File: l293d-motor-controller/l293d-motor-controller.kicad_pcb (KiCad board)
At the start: 2 copper layers, 49.6 x 66 mm, 19 parts, among them M1 Motor_DC, M2 Motor_DC, U1 LM7805, U2 L293D, U3 74HC04

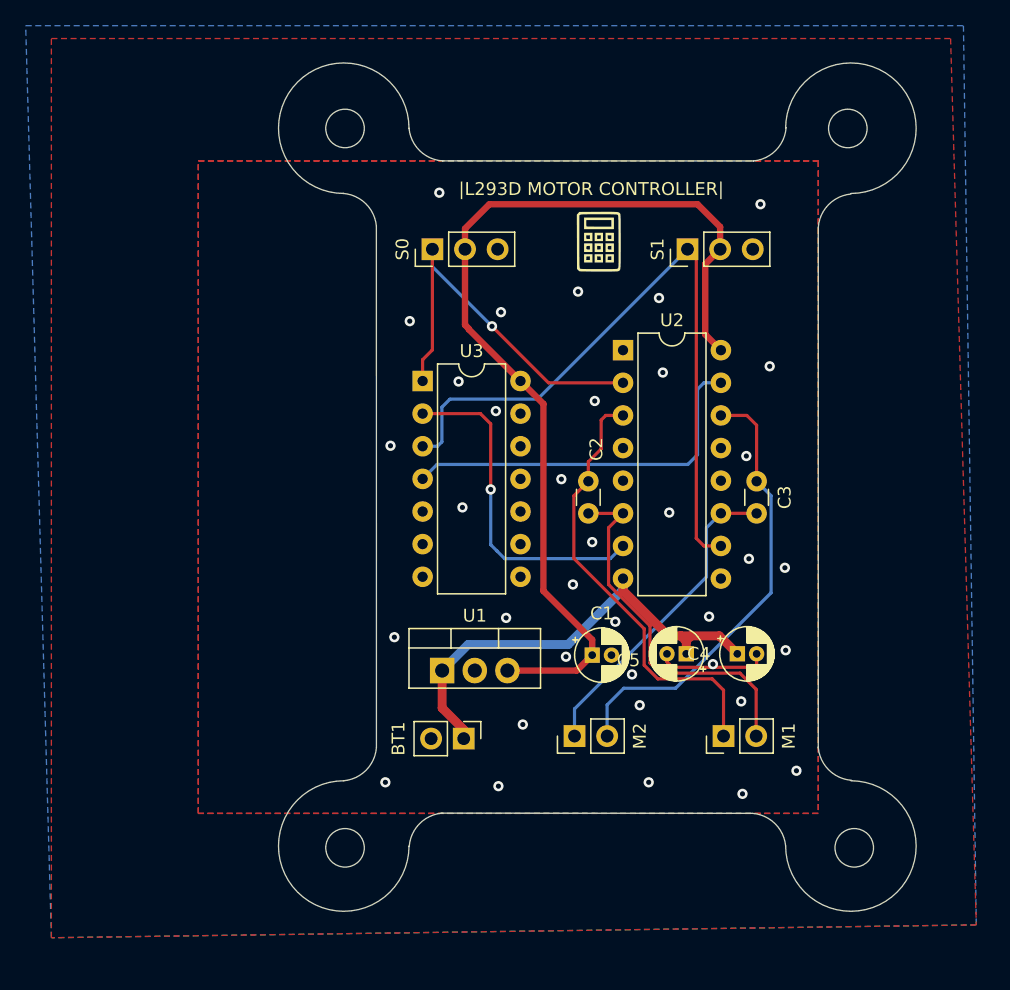
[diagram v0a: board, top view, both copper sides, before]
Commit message: project 3 / l293d motor driver / design improved
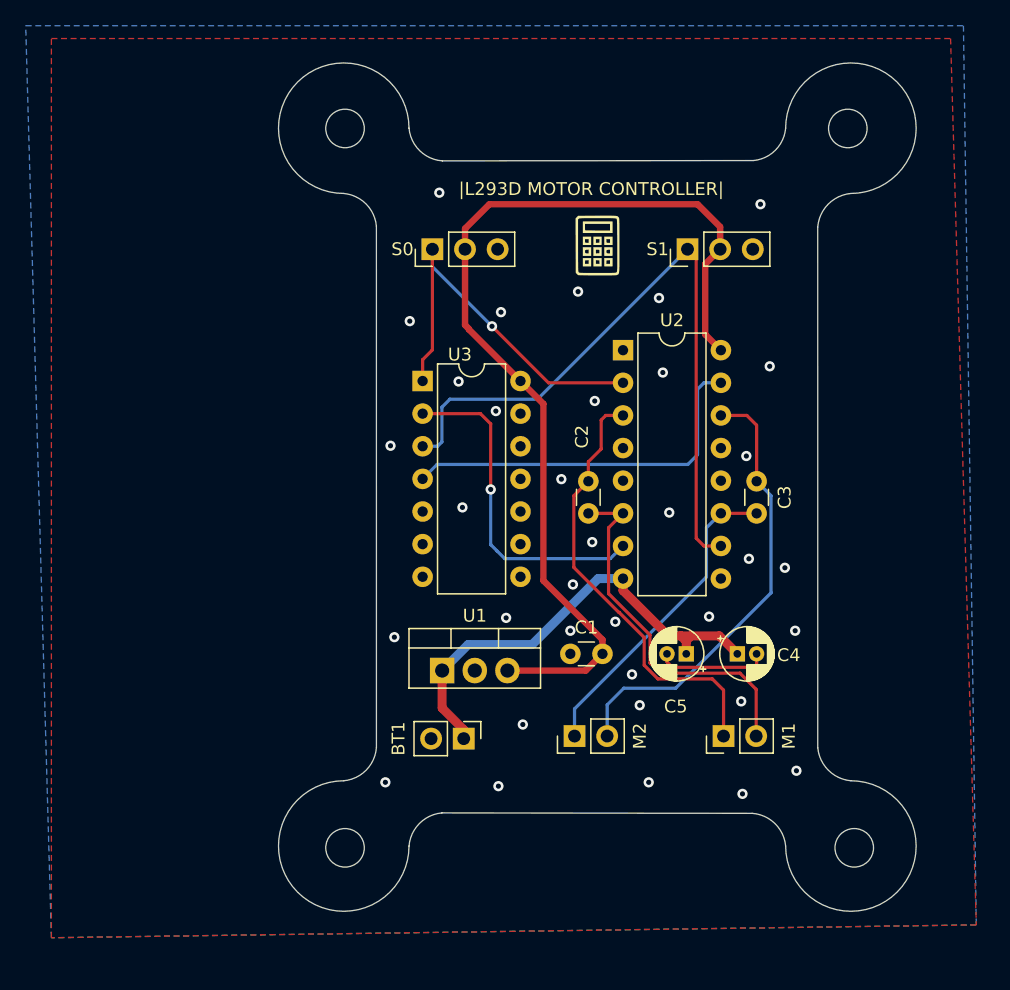
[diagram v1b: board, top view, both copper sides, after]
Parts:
- C1: value C_Polarized -> 100n; footprint Capacitor_THT:CP_Radial_D4.0mm_P1.50mm -> Capacitor_THT:C_Disc_D3.0mm_W1.6mm_P2.50mm
- C2, C3: value C -> 0.01u
- C4: value C_Polarized -> 10u
- C5: value C_Polarized -> 100u
- moved G*** 8.01 mm to (122.3, 122.3), turned to 180 degrees
- moved C1 1.70 mm to (120.4, 134.9)
- moved G*** 0.32 mm to (122.5, 103.1)
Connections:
- C1 pad 1: /5V -> /GND
- C1 pad 2: /GND -> /5V
- C2 pad 2: /VCC -> Net-(M1--)
- M1 pad 2: /VCC -> Net-(M1--)
- U2 pad 6: /VCC -> Net-(M1--)
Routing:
- net /VCC: track 66.5 -> 37.1 mm
- net Net-(M1--): track 0.00 -> 28.9 mm
- net /5V: track 77.1 -> 78.1 mm
- net /GND: track 8.92 -> 8.71 mm, vias 36 -> 35
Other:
- outline, holes or cut-outs redrawn

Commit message: project 3 / l293d motor driver / layout improvement
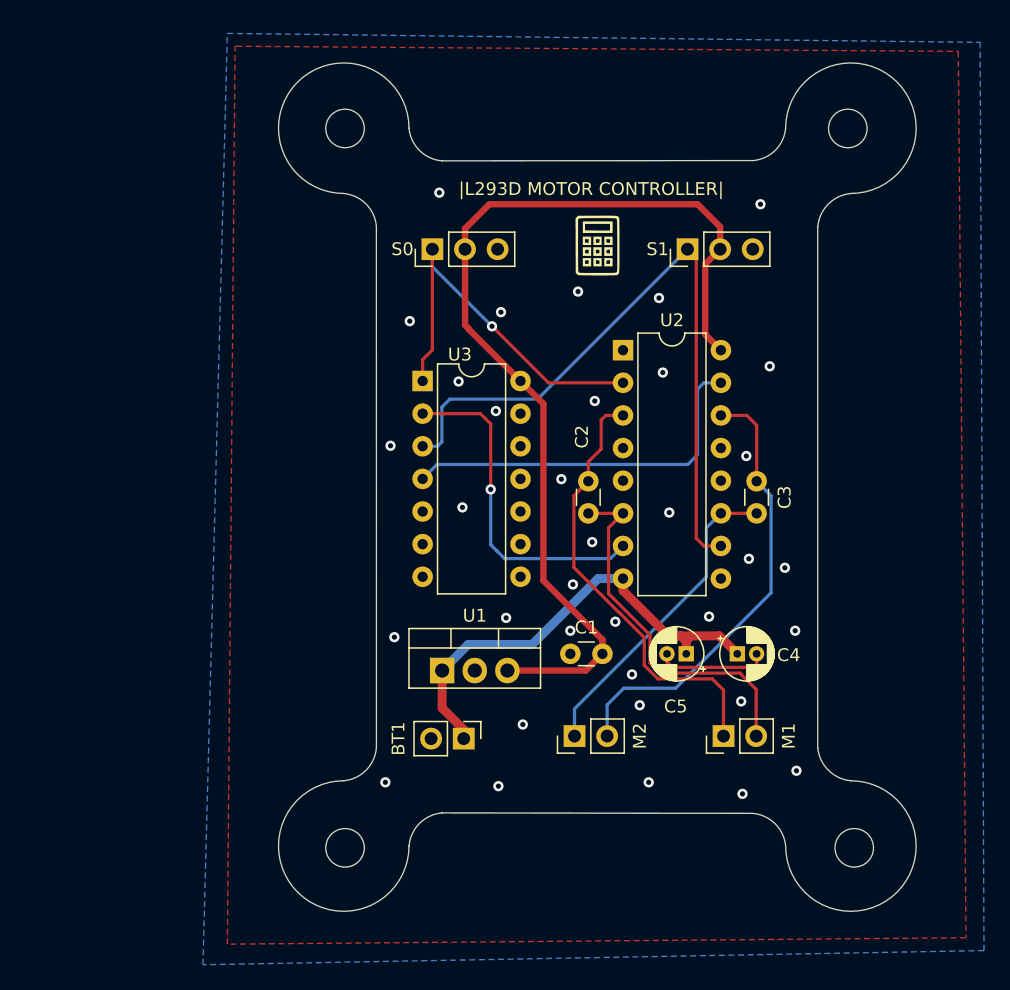
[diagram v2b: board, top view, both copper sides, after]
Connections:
- net /5V renamed +5V
- net /GND renamed GND
- net /VCC renamed +9V
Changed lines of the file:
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@@
   )
   (net 0 "")
-  (net 1 "/VCC")
-  (net 2 "/GND")
+  (net 1 "+9V")
+  (net 2 "GND")
   (net 3 "Net-(M1-+)")
   (net 4 "Net-(M2-+)")
@@
   (net 16 "unconnected-(U3-Q6-Pad12)")
   (net 17 "unconnected-(U3-Q7-Pad13)")
-  (net 18 "/5V")
+  (net 18 "+5V")
   (net 19 "unconnected-(U2-EN3,4-Pad9)")
   (net 20 "unconnected-(U2-EN1,2-Pad1)")
@@
       (stroke (width 0.1) (type solid)) (layer "F.Fab"))
     (pad "1" thru_hole rect (at 0 0) (size 1.905 2) (drill 1.1) (layers "*.Cu" "*.Mask")
-      (net 1 "/VCC") (pinfunction "IN") (pintype "power_in"))
+      (net 1 "+9V") (pinfunction "IN") (pintype "power_in"))
     (pad "2" thru_hole oval (at 2.54 0) (size 1.905 2) (drill 1.1) (layers "*.Cu" "*.Mask")
-      (net 2 "/GND") (pinfunction "GND") (pintype "power_in"))
+      (net 2 "GND") (pinfunction "GND") (pintype "power_in"))
     (pad "3" thru_hole oval (at 5.08 0) (size 1.905 2) (drill 1.1) (layers "*.Cu" "*.Mask")
-      (net 18 "/5V") (pinfunction "OUT") (pintype "power_out"))
+      (net 18 "+5V") (pinfunction "OUT") (pintype "power_out"))
     (model "${KICAD6_3DMODEL_DIR}/Package_TO_SOT_THT.3dshapes/TO-220-3_Vertical.wrl"
       (offset (xyz 0 0 0))
@@
       (stroke (width 0.1) (type solid)) (layer "F.Fab"))
     (pad "1" thru_hole rect (at 0 0 270) (size 1.7 1.7) (drill 1) (layers "*.Cu" "*.Mask")
-      (net 1 "/VCC") (pinfunction "+") (pintype "passive"))
+      (net 1 "+9V") (pinfunction "+") (pintype "passive"))
     (pad "2" thru_hole oval (at 0 2.54 270) (size 1.7 1.7) (drill 1) (layers "*.Cu" "*.Mask")
-      (net 2 "/GND") (pinfunction "-") (pintype "passive"))
+      (net 2 "GND") (pinfunction "-") (pintype "passive"))
     (model "${KICAD6_3DMODEL_DIR}/Connector_PinHeader_2.54mm.3dshapes/PinHeader_1x02_P2.54mm_Vertical.wrl"
       (offset (xyz 0 0 0))
@@
       (stroke (width 0.1) (type solid)) (fill none) (layer "F.Fab"))
     (pad "1" thru_hole rect (at 0 0 180) (size 1.2 1.2) (drill 0.6) (layers "*.Cu" "*.Mask")
-      (net 1 "/VCC") (pintype "passive"))
+      (net 1 "+9V") (pintype "passive"))
     (pad "2" thru_hole circle (at 1.5 0 180) (size 1.2 1.2) (drill 0.6) (layers "*.Cu" "*.Mask")
-      (net 2 "/GND") (pintype "passive"))
+      (net 2 "GND") (pintype "passive"))
     (model "${KICAD6_3DMODEL_DIR}/Capacitor_THT.3dshapes/CP_Radial_D4.0mm_P1.50mm.wrl"
       (offset (xyz 0 0 0))
@@
       (stroke (width 0.1) (type solid)) (layer "F.Fab"))
     (pad "1" thru_hole circle (at 0 0) (size 1.6 1.6) (drill 0.8) (layers "*.Cu" "*.Mask")
-      (net 2 "/GND") (pintype "passive"))
+      (net 2 "GND") (pintype "passive"))
     (pad "2" thru_hole circle (at 2.5 0) (size 1.6 1.6) (drill 0.8) (layers "*.Cu" "*.Mask")
-      (net 18 "/5V") (pintype "passive"))
+      (net 18 "+5V") (pintype "passive"))
     (model "${KICAD6_3DMODEL_DIR}/Capacitor_THT.3dshapes/C_Disc_D3.0mm_W1.6mm_P2.50mm.wrl"
       (offset (xyz 0 0 0))
@@
       (net 11 "unconnected-(U3-Q3-Pad6)") (pinfunction "Q3") (pintype "output+no_connect"))
     (pad "7" thru_hole oval (at 0 15.24) (size 1.6 1.6) (drill 0.8) (layers "*.Cu" "*.Mask")
-      (net 2 "/GND") (pinfunction "GND") (pintype "power_in"))
+      (net 2 "GND") (pinfunction "GND") (pintype "power_in"))
     (pad "8" thru_hole oval (at 7.62 15.24) (size 1.6 1.6) (drill 0.8) (layers "*.Cu" "*.Mask")
       (net 12 "unconnected-(U3-CP-Pad8)") (pinfunction "CP") (pintype "input+no_connect"))
@@
       (net 17 "unconnected-(U3-Q7-Pad13)") (pinfunction "Q7") (pintype "output+no_connect"))
     (pad "14" thru_hole oval (at 7.62 0) (size 1.6 1.6) (drill 0.8) (layers "*.Cu" "*.Mask")
-      (net 18 "/5V") (pinfunction "VCC") (pintype "power_in"))
+      (net 18 "+5V") (pinfunction "VCC") (pintype "power_in"))
     (model "${KICAD6_3DMODEL_DIR}/Package_DIP.3dshapes/DIP-14_W7.62mm.wrl"
       (offset (xyz 0 0 0))
@@
       (net 7 "/I3") (pinfunction "Pin_1") (pintype "passive"))
     (pad "2" thru_hole oval (at 0 2.54 90) (size 1.7 1.7) (drill 1) (layers "*.Cu" "*.Mask")
-      (net 18 "/5V") (pinfunction "Pin_2") (pintype "passive"))
+      (net 18 "+5V") (pinfunction "Pin_2") (pintype "passive"))
     (pad "3" thru_hole oval (at 0 5.08 90) (size 1.7 1.7) (drill 1) (layers "*.Cu" "*.Mask")
-      (net 2 "/GND") (pinfunction "Pin_3") (pintype "passive"))
+      (net 2 "GND") (pinfunction "Pin_3") (pintype "passive"))
     (model "${KICAD6_3DMODEL_DIR}/Connector_PinHeader_2.54mm.3dshapes/PinHeader_1x03_P2.54mm_Vertical.wrl"
       (offset (xyz 0 0 0))
@@
       (stroke (width 0.1) (type solid)) (fill none) (layer "F.Fab"))
     (pad "1" thru_hole rect (at 0 0) (size 1.2 1.2) (drill 0.6) (layers "*.Cu" "*.Mask")
-      (net 1 "/VCC") (pintype "passive"))
+      (net 1 "+9V") (pintype "passive"))
     (pad "2" thru_hole circle (at 1.5 0) (size 1.2 1.2) (drill 0.6) (layers "*.Cu" "*.Mask")
-      (net 2 "/GND") (pintype "passive"))
+      (net 2 "GND") (pintype "passive"))
     (model "${KICAD6_3DMODEL_DIR}/Capacitor_THT.3dshapes/CP_Radial_D4.0mm_P1.50mm.wrl"
       (offset (xyz 0 0 0))
@@
       (net 3 "Net-(M1-+)") (pinfunction "1Y") (pintype "output"))
     (pad "4" thru_hole oval (at 0 7.62) (size 1.6 1.6) (drill 0.8) (layers "*.Cu" "*.Mask")
-      (net 2 "/GND") (pinfunction "GND") (pintype "power_in"))
+      (net 2 "GND") (pinfunction "GND") (pintype "power_in"))
     (pad "5" thru_hole oval (at 0 10.16) (size 1.6 1.6) (drill 0.8) (layers "*.Cu" "*.Mask")
-      (net 2 "/GND") (pinfunction "GND") (pintype "power_in"))
+      (net 2 "GND") (pinfunction "GND") (pintype "power_in"))
     (pad "6" thru_hole oval (at 0 12.7) (size 1.6 1.6) (drill 0.8) (layers "*.Cu" "*.Mask")
       (net 21 "Net-(M1--)") (pinfunction "2Y") (pintype "output"))
@@
       (net 8 "/I2") (pinfunction "2A") (pintype "input"))
     (pad "8" thru_hole oval (at 0 17.78) (size 1.6 1.6) (drill 0.8) (layers "*.Cu" "*.Mask")
-      (net 1 "/VCC") (pinfunction "VCC2") (pintype "power_in"))
+      (net 1 "+9V") (pinfunction "VCC2") (pintype "power_in"))
     (pad "9" thru_hole oval (at 7.62 17.78) (size 1.6 1.6) (drill 0.8) (layers "*.Cu" "*.Mask")
       (net 19 "unconnected-(U2-EN3,4-Pad9)") (pinfunction "EN3,4") (pintype "input+no_connect"))
@@
       (net 4 "Net-(M2-+)") (pinfunction "3Y") (pintype "output"))
     (pad "12" thru_hole oval (at 7.62 10.16) (size 1.6 1.6) (drill 0.8) (layers "*.Cu" "*.Mask")
-      (net 2 "/GND") (pinfunction "GND") (pintype "power_in"))
+      (net 2 "GND") (pinfunction "GND") (pintype "power_in"))
     (pad "13" thru_hole oval (at 7.62 7.62) (size 1.6 1.6) (drill 0.8) (layers "*.Cu" "*.Mask")
-      (net 2 "/GND") (pinfunction "GND") (pintype "power_in"))
+      (net 2 "GND") (pinfunction "GND") (pintype "power_in"))
     (pad "14" thru_hole oval (at 7.62 5.08) (size 1.6 1.6) (drill 0.8) (layers "*.Cu" "*.Mask")
       (net 5 "Net-(M2--)") (pinfunction "4Y") (pintype "output"))
@@
       (net 9 "/I4") (pinfunction "4A") (pintype "input"))
     (pad "16" thru_hole oval (at 7.62 0) (size 1.6 1.6) (drill 0.8) (layers "*.Cu" "*.Mask")
-      (net 18 "/5V") (pinfunction "VCC1") (pintype "power_in"))
+      (net 18 "+5V") (pinfunction "VCC1") (pintype "power_in"))
     (model "${KICAD6_3DMODEL_DIR}/Package_DIP.3dshapes/DIP-16_W7.62mm.wrl"
       (offset (xyz 0 0 0))
@@
       (net 6 "/I1") (pinfunction "Pin_1") (pintype "passive"))
     (pad "2" thru_hole oval (at 0 2.54 90) (size 1.7 1.7) (drill 1) (layers "*.Cu" "*.Mask")
-      (net 18 "/5V") (pinfunction "Pin_2") (pintype "passive"))
+      (net 18 "+5V") (pinfunction "Pin_2") (pintype "passive"))
     (pad "3" thru_hole oval (at 0 5.08 90) (size 1.7 1.7) (drill 1) (layers "*.Cu" "*.Mask")
-      (net 2 "/GND") (pinfunction "Pin_3") (pintype "passive"))
+      (net 2 "GND") (pinfunction "Pin_3") (pintype "passive"))
     (model "${KICAD6_3DMODEL_DIR}/Connector_PinHeader_2.54mm.3dshapes/PinHeader_1x03_P2.54mm_Vertical.wrl"
       (offset (xyz 0 0 0))
@@
   (segment (start 123.375 130.213299) (end 123.375 125.085) (width 0.25) (layer "F.Cu") (net 21))
   (segment (start 121.8 123.965) (end 124.495 123.965) (width 0.25) (layer "F.Cu") (net 21))
-  (zone (net 2) (net_name "/GND") (layer "F.Cu") (hatch edge 0.5)
-    (priority 3)
+  (zone (net 2) (net_name "GND") (layer "F.Cu") (hatch edge 0.5)
     (connect_pads (clearance 0.5))
     (min_thickness 0.25) (filled_areas_thickness no)
@@
     (polygon
       (pts
-        (xy 80 87)
-        (xy 150 87)
-        (xy 152 156)
-        (xy 80 157)
+        (xy 94.4 87.6)
+        (xy 150.6 88)
+        (xy 151.2 157)
+        (xy 93.7 157.5)
+        (xy 94.3 87.6)
       )
     )
   )
-  (zone (net 2) (net_name "/GND") (layer "B.Cu") (hatch edge 0.5)
-    (priority 4)
+  (zone (net 2) (net_name "GND") (layer "B.Cu") (hatch edge 0.5)
+    (priority 1)
     (connect_pads (clearance 0.5))
     (min_thickness 0.25) (filled_areas_thickness no)
@@
     (polygon
       (pts
-        (xy 78 86)
-        (xy 151 86)
-        (xy 152 156)
-        (xy 80 157)
+        (xy 93.7 86.6)
+        (xy 152.3 87.3)
+        (xy 152.6 158)
+        (xy 91.8 159.1)
       )
     )

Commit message: project 3 / l293 motor driver / tracks reworked
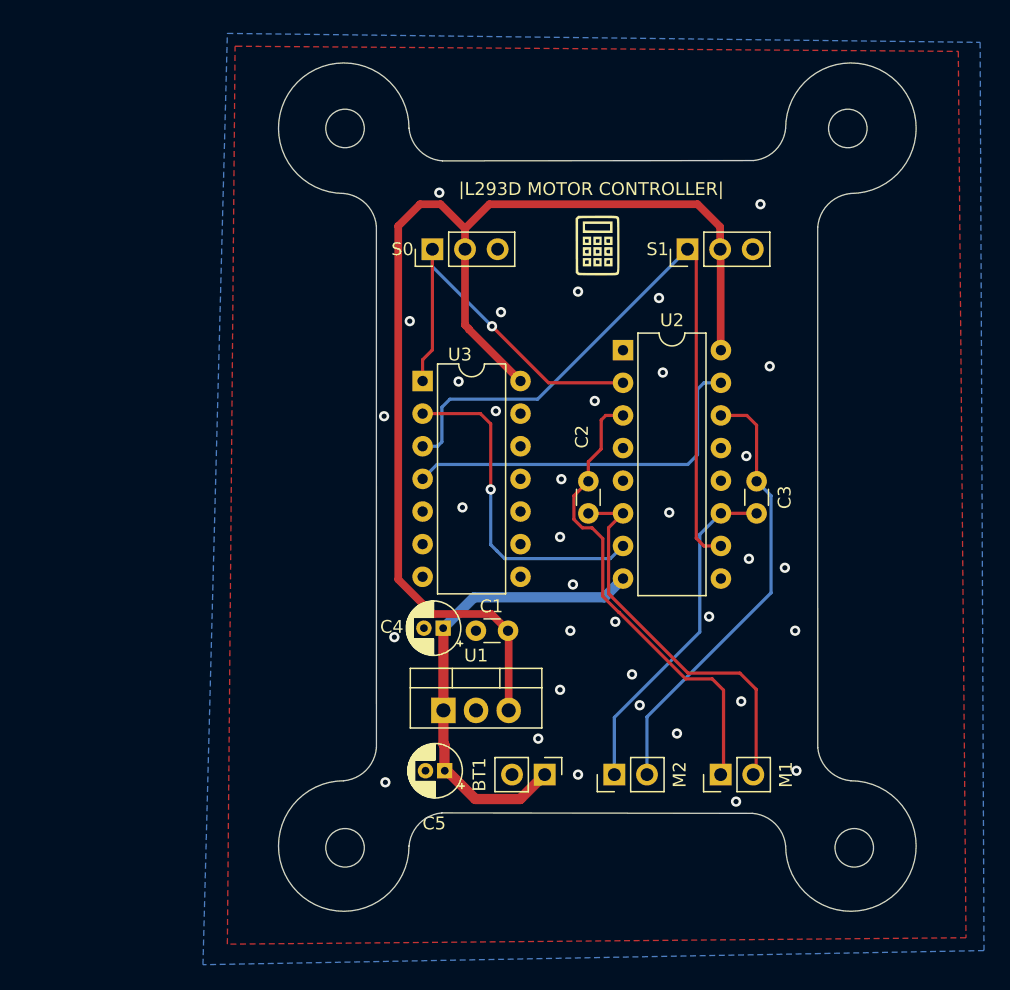
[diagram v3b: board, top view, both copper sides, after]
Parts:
- moved C4 23.0 mm to (110.5, 132.9), turned to 180 degrees
- moved C5 20.9 mm to (110.6, 144.0)
- moved C1 7.57 mm to (113.0, 133.1)
- moved BT1 6.89 mm to (118.4, 144.3)
- moved M2 4.31 mm to (123.8, 144.3)
- moved U1 3.10 mm to (110.5, 139.3)
- moved M1 3.01 mm to (132.1, 144.3)
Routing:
- net +5V: track 78.1 -> 96.0 mm
- net GND: track 8.71 -> 0.00 mm
- net Net-(M1-+): track 34.7 -> 36.9 mm
- net Net-(M1--): track 28.9 -> 30.7 mm
- net Net-(M2-+): track 24.8 -> 26.7 mm
- net +9V: track 37.1 -> 36.1 mm
- net Net-(M2--): track 35.4 -> 34.8 mm
